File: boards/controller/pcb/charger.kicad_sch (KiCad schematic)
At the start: 36 parts, among them J601 Conn_01x02_Socket

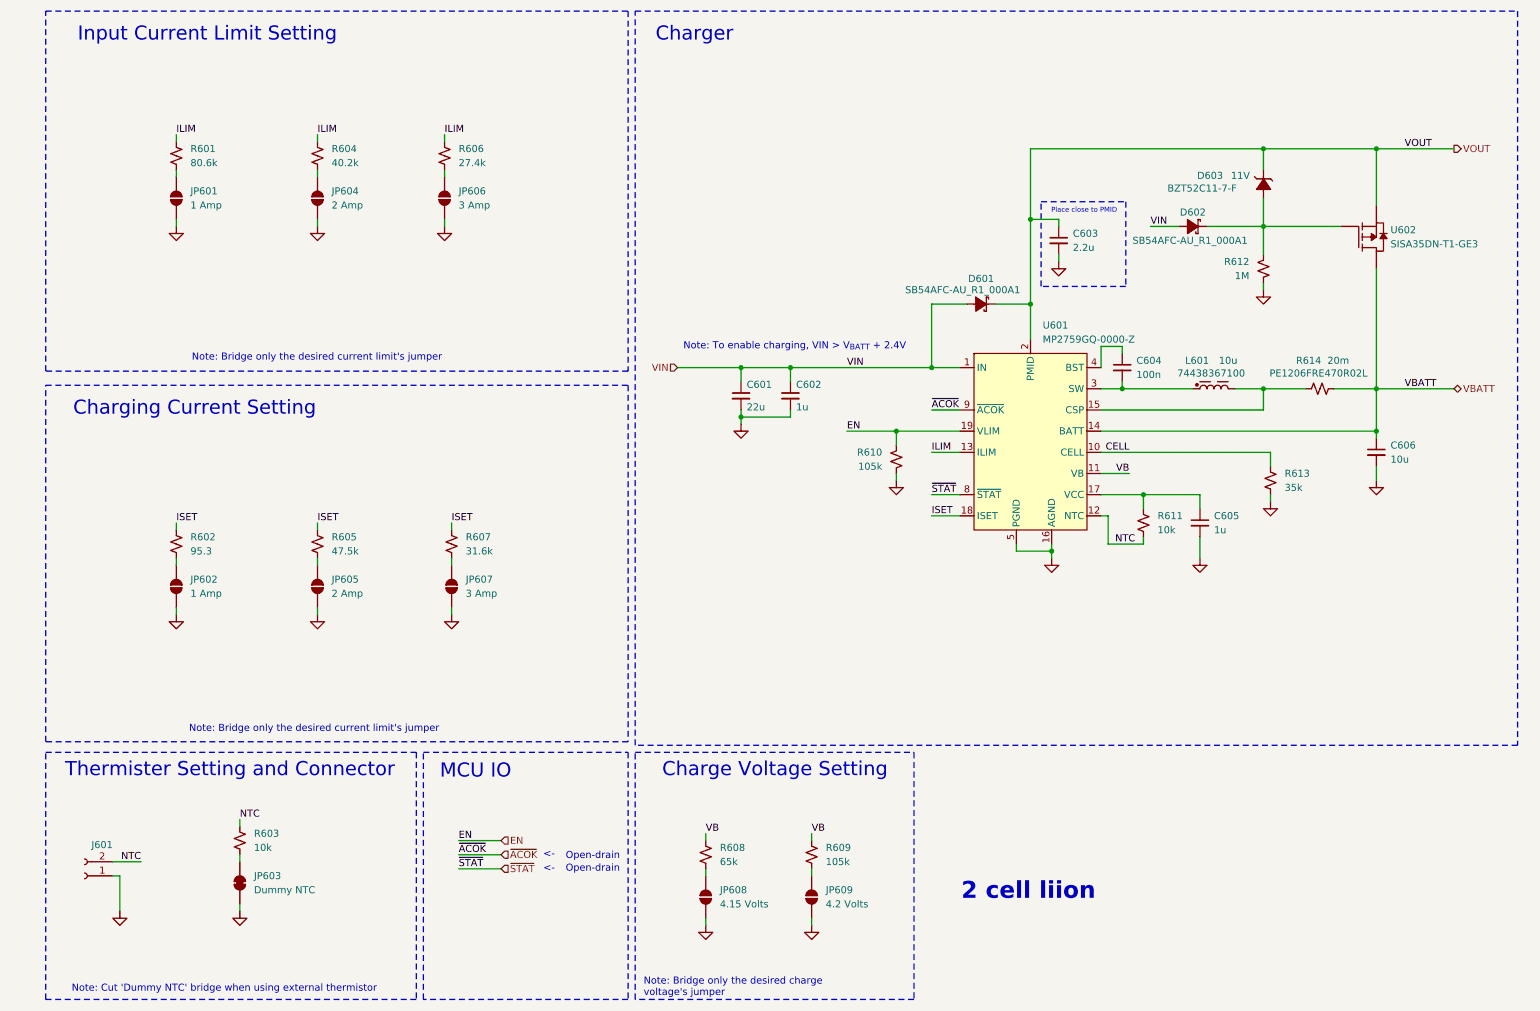
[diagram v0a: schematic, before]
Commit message: controller: pcb: Update schematic
Signed-off-by: Nicholas Loehrke <nicholasnloehrke@gmail.com>
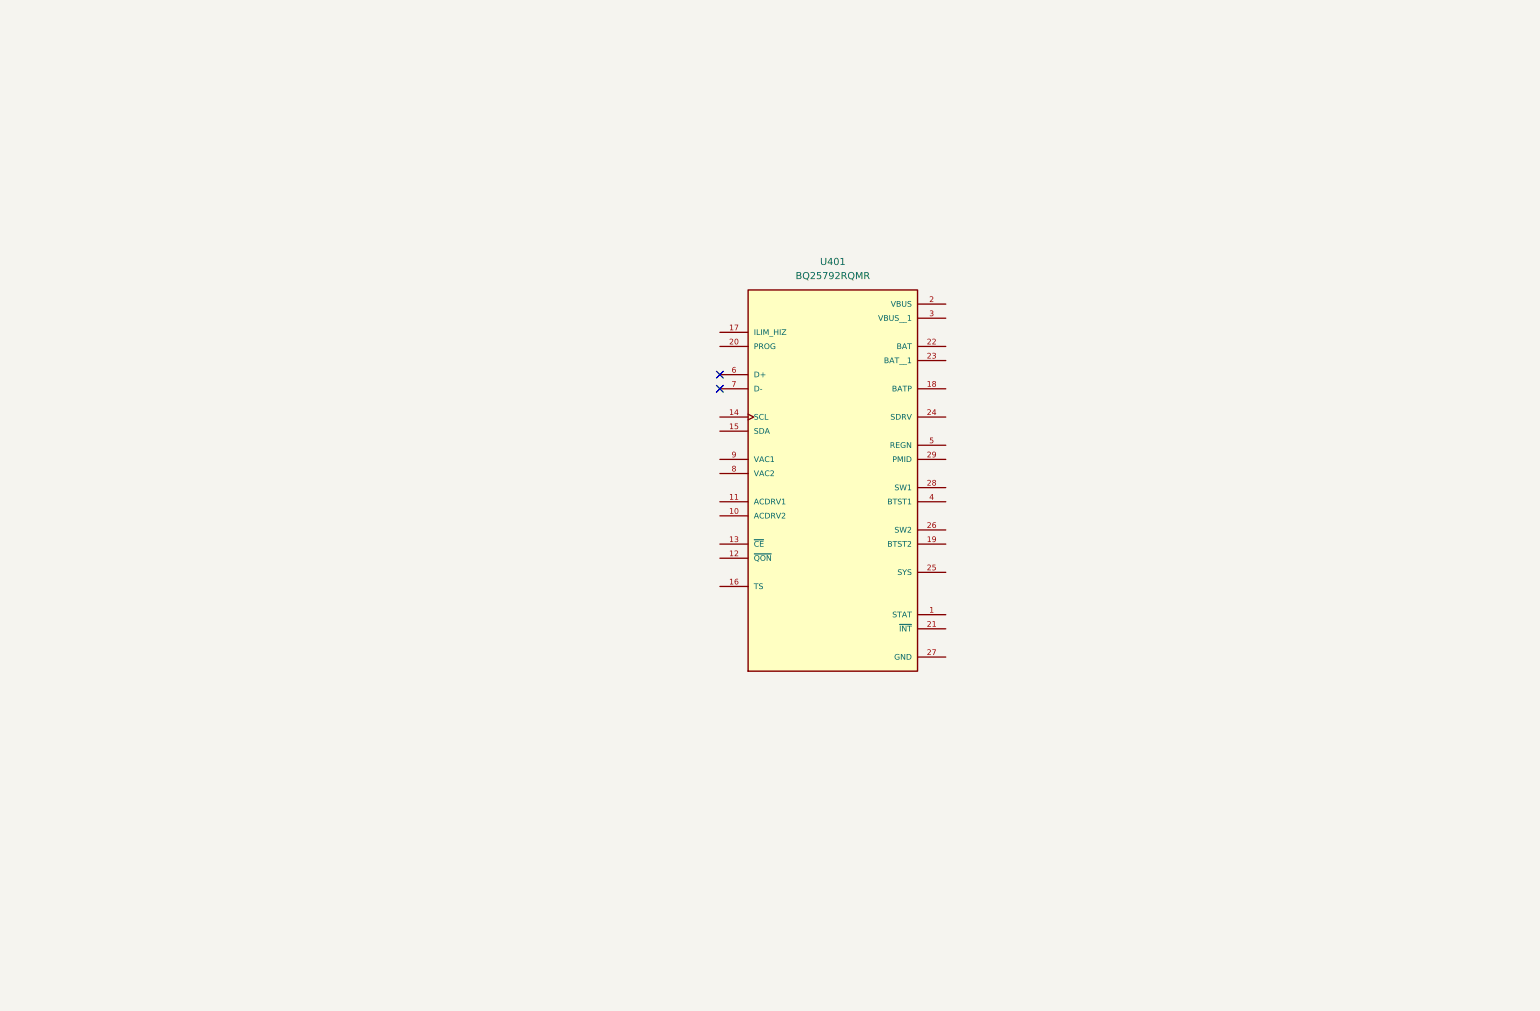
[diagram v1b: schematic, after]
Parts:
- removed C601: 22u, Capacitor_SMD:C_1206_3216Metric, symbol Device:C_Small
- removed C602, C605: 1u, Capacitor_SMD:C_0603_1608Metric, symbol Device:C_Small
- removed C603: 2.2u, Capacitor_SMD:C_1206_3216Metric, symbol Device:C_Small
- removed C604: 100n, Capacitor_SMD:C_0603_1608Metric, symbol Device:C_Small
- removed C606: 10u, Capacitor_SMD:C_0805_2012Metric, symbol Device:C_Small
- removed D601, D602: SB54AFC-AU_R1_000A1, DIODE_SB54AFC-AU_R1_000A1_PNJ, symbol SB54AFC-AU_R1_000A1:SB54AFC-AU_R1_000A1
- removed D603: 11V, BZT52C11-7-F:BZT52C11-7-F, symbol BZT52C11-7-F:BZT52C11-7-F
- removed J601: Conn_01x02_Socket, Connector_JST:JST_XH_B2B-XH-A_1x02_P2.50mm_Vertical, symbol Connector:Conn_01x02_Socket
- removed JP601, JP602: 1 Amp, Jumper:SolderJumper-2_P1.3mm_Open_RoundedPad1.0x1.5mm, symbol Jumper:SolderJumper_2_Open
- removed JP603: Dummy NTC, symbol Jumper:SolderJumper_2_Bridged
- removed JP604, JP605: 2 Amp, Jumper:SolderJumper-2_P1.3mm_Open_RoundedPad1.0x1.5mm, symbol Jumper:SolderJumper_2_Open
- removed JP606, JP607: 3 Amp, Jumper:SolderJumper-2_P1.3mm_Open_RoundedPad1.0x1.5mm, symbol Jumper:SolderJumper_2_Open
- removed JP608: 4.15 Volts, Jumper:SolderJumper-2_P1.3mm_Open_RoundedPad1.0x1.5mm, symbol Jumper:SolderJumper_2_Open
- removed JP609: 4.2 Volts, Jumper:SolderJumper-2_P1.3mm_Open_RoundedPad1.0x1.5mm, symbol Jumper:SolderJumper_2_Open
- removed L601: 10u, 74438367100:74438367100, symbol 74438367100:74438367100
- removed R601: 80.6k, Resistor_SMD:R_0603_1608Metric, symbol Device:R_Small_US
- removed R602: 95.3, Resistor_SMD:R_0603_1608Metric, symbol Device:R_Small_US
- removed R603, R611: 10k, Resistor_SMD:R_0603_1608Metric, symbol Device:R_Small_US
- removed R604: 40.2k, Resistor_SMD:R_0603_1608Metric, symbol Device:R_Small_US
- removed R605: 47.5k, Resistor_SMD:R_0603_1608Metric, symbol Device:R_Small_US
- removed R606: 27.4k, Resistor_SMD:R_0603_1608Metric, symbol Device:R_Small_US
- removed R607: 31.6k, Resistor_SMD:R_0603_1608Metric, symbol Device:R_Small_US
- removed R608: 65k, Resistor_SMD:R_0603_1608Metric, symbol Device:R_Small_US
- removed R609, R610: 105k, Resistor_SMD:R_0603_1608Metric, symbol Device:R_Small_US
- removed R612: 1M, Resistor_SMD:R_0603_1608Metric, symbol Device:R_Small_US
- removed R613: 35k, Resistor_SMD:R_0603_1608Metric, symbol Device:R_Small_US
- removed R614: 20m, PE1206FRE470R02L:PE1206FRE470R02L, symbol PE1206FRE470R02L:PE1206FRE470R02L
- removed U601: ~, MP2759GQ-0000-Z:MP2759GQ-0000-Z, symbol MP2759GQ-0000-Z:MP2759GQ-0000-Z
- removed U602: ~, SISA35DN-T1-GE3:SISA35DN-T1-GE3, symbol SISA35DN-T1-GE3:SISA35DN-T1-GE3
- added U401: BQ25792RQMR, BQ25792RQMR:QFN40P400X400X100-29N, symbol BQ25792RQMR:BQ25792RQMR
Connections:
- no-connect marks 0 -> 2
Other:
- note removed: "2 cell liion"
- note removed: "<-"
- note removed: "Charge Voltage Setting"
- note removed: "Charger"
- note removed: "Charging Current Setting"
- note removed: "Input Current Limit Setting"
- note removed: "MCU IO"
- note removed: "Note: Bridge only the desired charge voltage's jumper"
- note removed: "Note: Bridge only the desired current limit's jumper"
- note removed: "Note: Cut 'Dummy NTC' bridge when using external thermistor"
- note removed: "Note: To enable charging, VIN > V_{BATT} + 2.4V"
- note removed: "Open-drain"
- note removed: "Place close to PMID"
- note removed: "Thermister Setting and Connector"

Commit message: controller: pcb: Update schematic
Signed-off-by: Nicholas Loehrke <nicholasnloehrke@gmail.com>
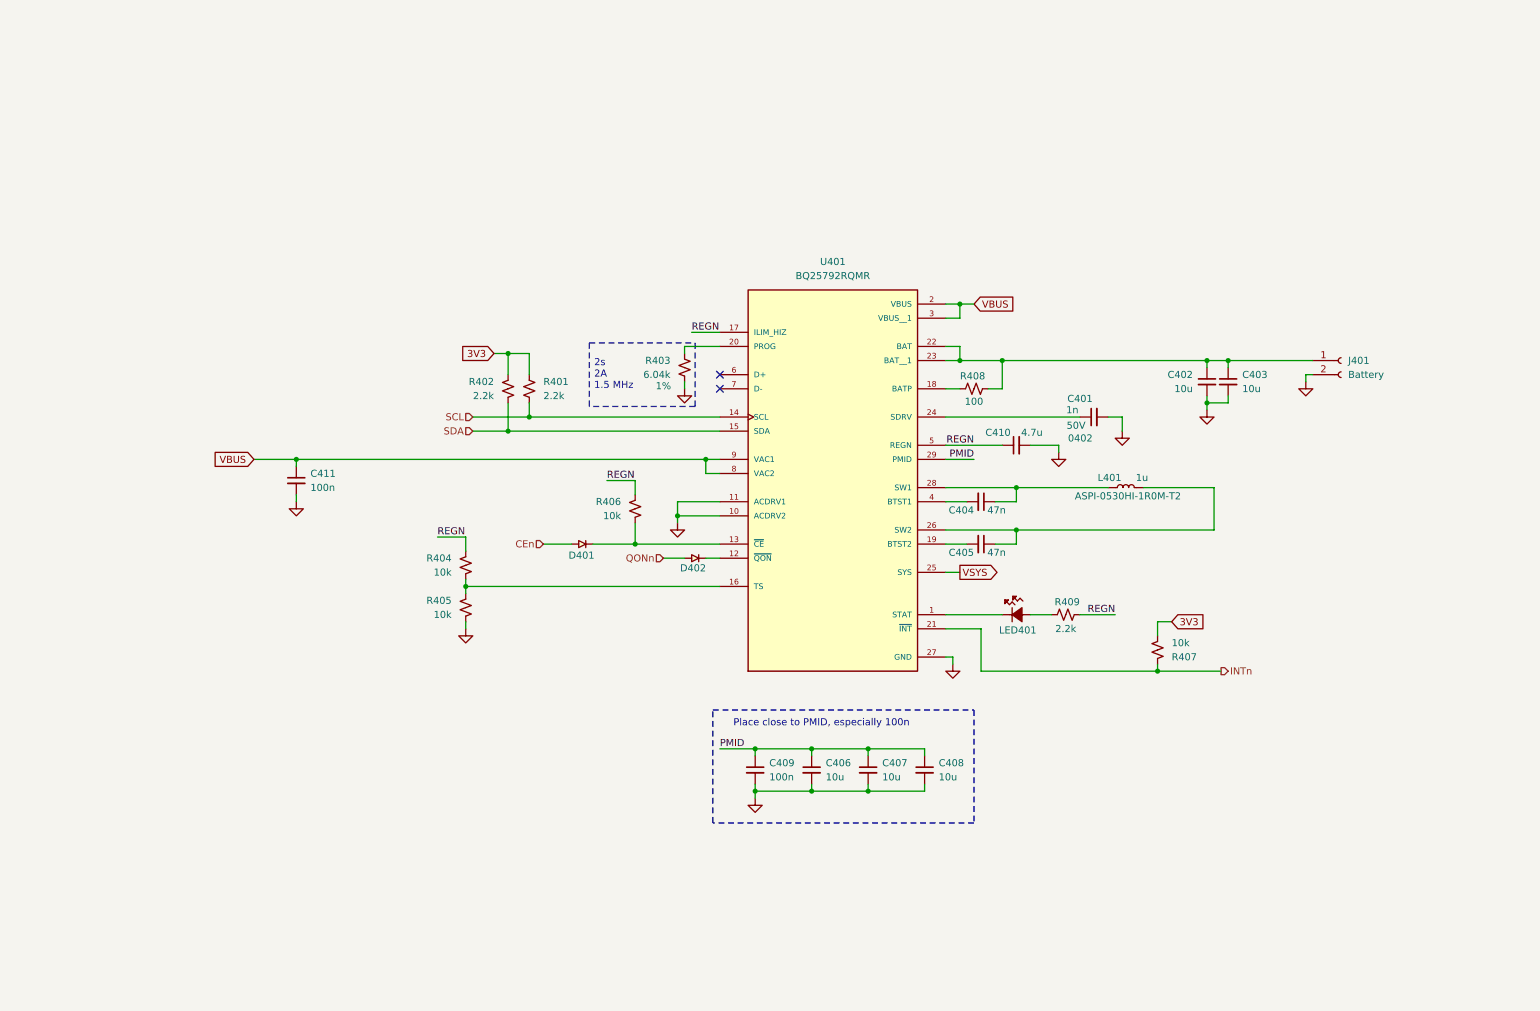
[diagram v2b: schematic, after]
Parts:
- added C401: 1n, symbol Device:C_Small
- added C402, C403, C406, C407, C408: 10u, symbol Device:C_Small
- added C404, C405: 47n, symbol Device:C_Small
- added C409, C411: 100n, symbol Device:C_Small
- added C410: 4.7u, symbol Device:C_Small
- added D401, D402: CUS10S30_H3F, USC_TOS, symbol CUS10S30_H3F:CUS10S30_H3F
- added J401: Battery, symbol Connector:Conn_01x02_Socket
- added L401: 1u, ASPI-0530HI-1R0M-T2:IND_ASPI-0530HI-1R0M-T2, symbol ASPI-0530HI-1R0M-T2:ASPI-0530HI-1R0M-T2
- added LED401: B1911PG--20D000514U1930, LED_B1911PG--20D000514U1930_HVK, symbol B1911PG--20D000514U1930:B1911PG--20D000514U1930
- added R401, R402, R409: 2.2k, symbol Device:R_Small_US
- added R403: 6.04k, symbol Device:R_Small_US
- added R404, R405, R406, R407: 10k, symbol Device:R_Small_US
- added R408: 100, symbol Device:R_Small_US
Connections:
- net at U401.1 (STAT): now also LED401.1
- net GND: now reaches U401.10 (ACDRV2)
- net GND: now also U401.11 (ACDRV1), U401.27 (GND), C401.2, C402.2, C403.2, C406.2, C407.2, C408.2, C409.2, C410.2, C411.2, J401.2 (Pin_2), R403.2, R405.2
- net at U401.12 (~{QON}): now also D402.1
- net at U401.13 (~{CE}): now also D401.1, R406.2
- net SCL: now reaches U401.14 (SCL)
- net SCL: now also R401.1
- net SDA: now reaches U401.15 (SDA)
- net SDA: now also R402.1
- net at U401.16 (TS): now also R404.2, R405.1
- net REGN: now reaches U401.17 (ILIM_HIZ)
- net REGN: now also U401.5 (REGN), C410.1, R404.1, R406.1, R409.2
- net at U401.18 (BATP): now also R408.1
- net at U401.19 (BTST2): now also C405.2
- net VBUS: now reaches U401.2 (VBUS)
- net VBUS: now also U401.3 (VBUS__1), U401.8 (VAC2), U401.9 (VAC1), C411.1
- net at U401.20 (PROG): now also R403.1
- net INTn: now reaches U401.21 (~{INT})
- net INTn: now also R407.1
- net at U401.22 (BAT): now also U401.23 (BAT__1), C402.1, C403.1, J401.1 (Pin_1), R408.2
- net at U401.24 (SDRV): now also C401.1
- net VSYS: now reaches U401.25 (SYS)
- net at U401.26 (SW2): now also C405.1, L401.2
- net at U401.28 (SW1): now also C404.1, L401.1
- net PMID: now reaches U401.29 (PMID)
- net PMID: now also C406.1, C407.1, C408.1, C409.1
- net at U401.4 (BTST1): now also C404.2
- new net: LED401.2, R409.1
- new net 3V3: R401.2, R402.2, R407.2
- new net CEn: D401.2
- new net QONn: D402.2
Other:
- note added: "2s 2A 1.5 MHz"
- note added: "Place close to PMID, especially 100n"

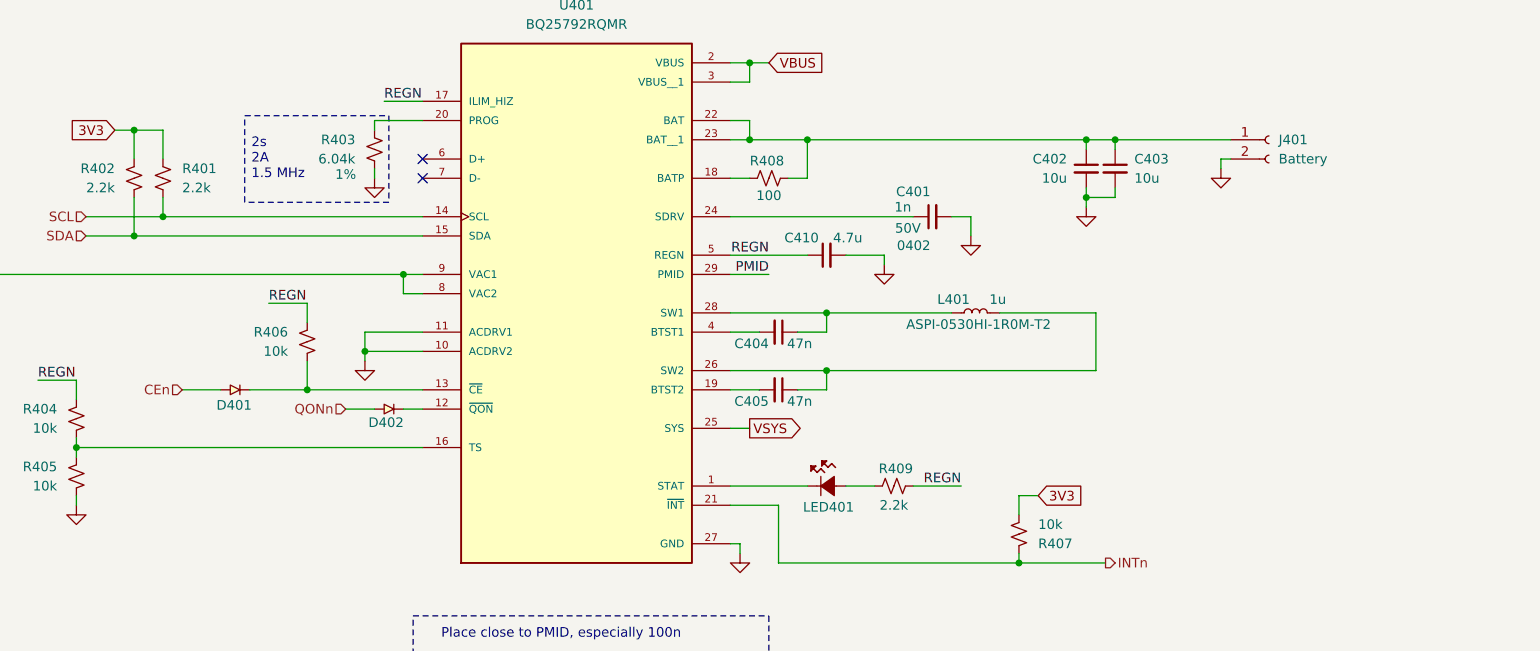
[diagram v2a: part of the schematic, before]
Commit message: controller: pcb: Update schematic
Signed-off-by: Nicholas Loehrke <nicholasnloehrke@gmail.com>
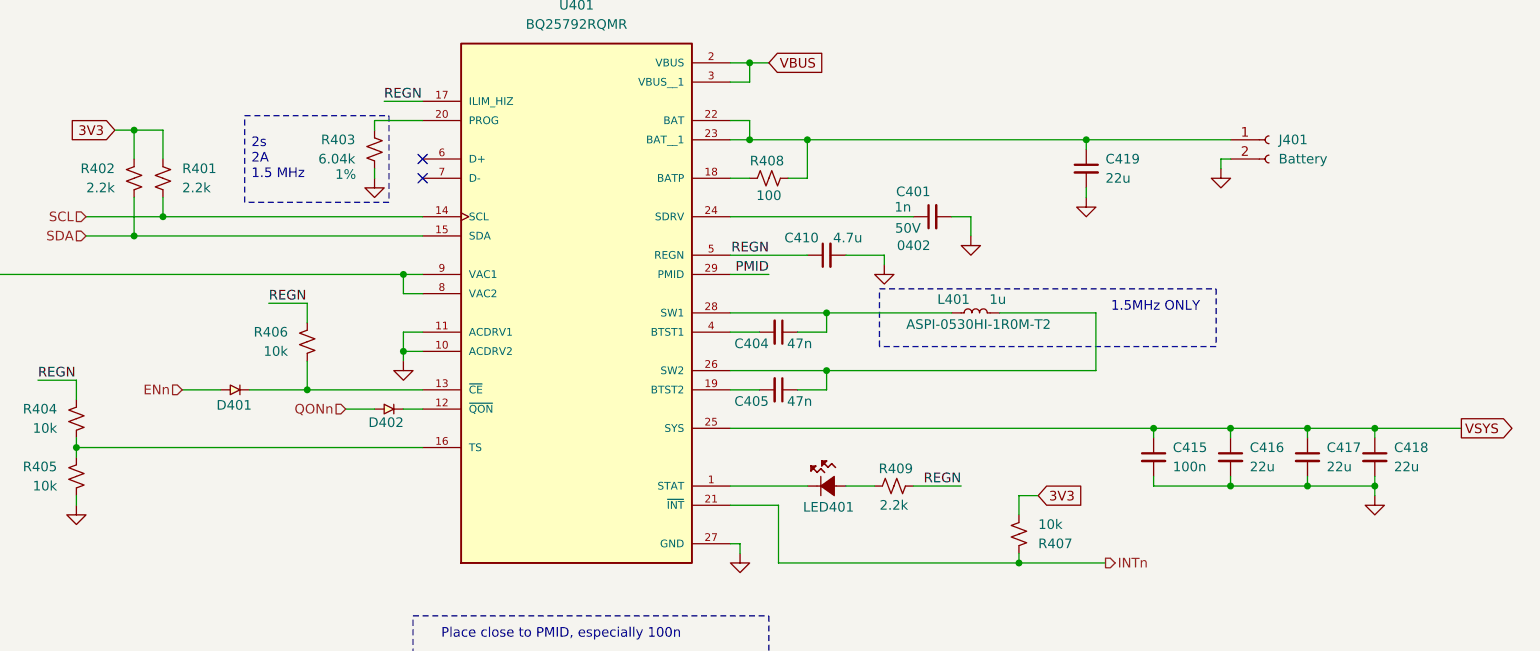
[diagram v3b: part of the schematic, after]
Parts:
- removed C402, C403: 10u, symbol Device:C_Small
- added C415: 100n, symbol Device:C_Small
- added C416, C417, C418, C419: 22u, symbol Device:C_Small
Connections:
- net GND: now also C415.2, C416.2, C417.2, C418.2, C419.2
- net VSYS: now also C415.1, C416.1, C417.1, C418.1
- net at J401.1 (Pin_1), R408.2, U401.22 (BAT)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: now also C419.1
- net CEn renamed ENn
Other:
- note added: "1.5MHz ONLY"
